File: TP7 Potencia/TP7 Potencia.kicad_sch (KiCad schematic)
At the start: 55 parts, among them J1 Input, Q1 IRF830PBF, Q2 IRF830PBF, Q3 IRF830PBF, Q4 IRF830PBF, Q5 BC337, Q6 BC337, Q7 2N7000, Q8 2N7000, SW1 SW_Push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

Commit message: Agregado footprints
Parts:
- removed U4: CD4049UBEE4, CD4049UBEE4:DIP794W45P254L1969H508Q16, symbol CD4049:CD4049UBEE4
- added U6: CD40106BE, footprints:DIP794W45P254L1969H508Q14, symbol C40106:CD40106BE
- C1, C3, C6, C7: footprint (none) -> Capacitor_THT:CP_Radial_D6.3mm_P2.50mm
- C10, C2, C4, C5: footprint (none) -> Capacitor_THT:C_Disc_D3.0mm_W1.6mm_P2.50mm
- C8, C9: value 100p -> 500p; footprint (none) -> Capacitor_THT:C_Disc_D3.0mm_W1.6mm_P2.50mm
- D10: footprint (none) -> LED_THT:LED_D3.0mm
- D9: footprint (none) -> Diode_THT:D_DO-35_SOD27_P7.62mm_Horizontal
- J1: footprint (none) -> TerminalBlock_MetzConnect:TerminalBlock_MetzConnect_Type011_RT05502HBWC_1x02_P5.00mm_Horizontal
- Q1, Q2, Q3, Q4: footprint TO254P1052X465X1989-3 -> footprints:TO254P1052X465X1989-3
- R1, R10, R11, R12, R13, R14, R15, R16, R2, R3, R4, R5, R6, R9: footprint (none) -> Resistor_THT:R_Axial_DIN0207_L6.3mm_D2.5mm_P10.16mm_Horizontal
- R7, R8: value 5k8 -> 12k; footprint (none) -> Resistor_THT:R_Axial_DIN0207_L6.3mm_D2.5mm_P10.16mm_Horizontal
- RV1, RV2, RV3, RV4: footprint (none) -> Potentiometer_THT:Potentiometer_Bourns_3266Y_Vertical
- SW1: footprint (none) -> Button_Switch_THT:SW_Push_2P1T_Toggle_CK_PVA1xxH1xxxxxxV2
- U1: footprint (none) -> Package_DIP:DIP-16_W7.62mm_Socket_LongPads
- U5: footprint (none) -> Package_DIP:DIP-8_W7.62mm_Socket_LongPads
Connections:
- net 12V: now also U6.14 (VDD)
- net B: now also U6.3 (B)
- net D: now also U6.6 (I=~C), U6.9 (D)
- net E: now also U6.11 (E)
- net GND: now also U6.7 (VSS)
- net PWM: now also U6.1 (A), U6.5 (C)
- net PWM1: now also U6.4 (H=~B)
- net PWM2: now also U6.10 (K=~E)
- net at D8.2 (A), R8.1: now also U6.8 (J=~D)
- net at D7.2 (A), R7.1: now also U6.2 (G=~A)
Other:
- note removed: "AGREGAR FOOTPRINTS Y CHECKEAR BIEN QUE SEAN LOS CORRECTOS"
- moved on the sheet: C10, D10, Q5, Q6, Q7, Q8, R12, R13, R14, R15, R16, SW1

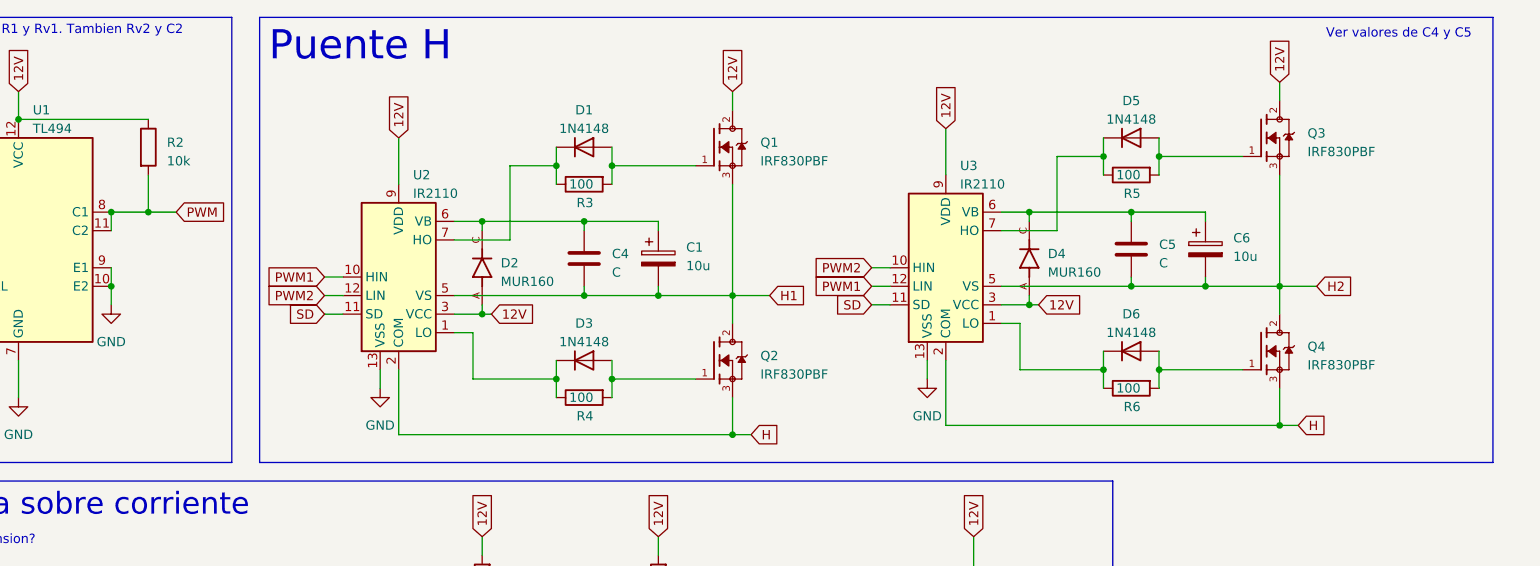
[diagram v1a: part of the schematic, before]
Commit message: Placement de componentes en el PCB
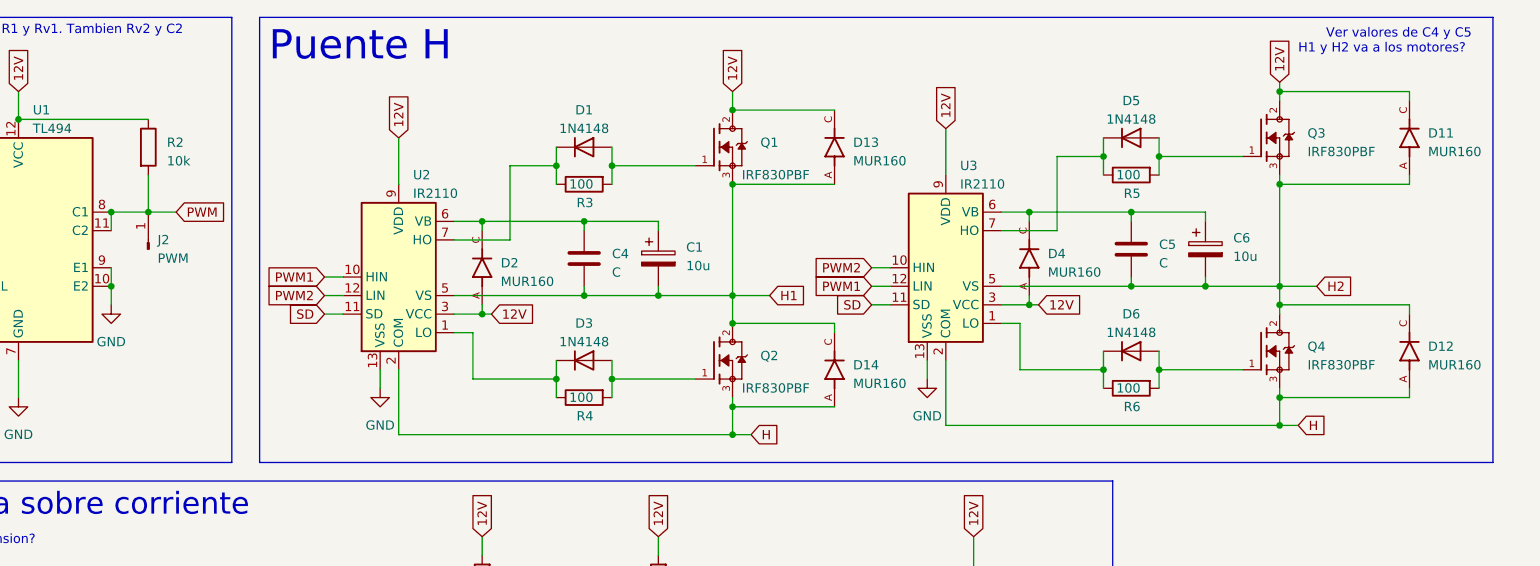
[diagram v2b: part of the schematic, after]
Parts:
- added D11, D12, D13, D14: MUR160, MUR160:DIOAD1300W80L670D310, symbol MUR160:MUR160
- added J2: PWM, Connector_PinSocket_2.54mm:PinSocket_1x01_P2.54mm_Vertical, symbol Connector:Conn_01x01_Pin
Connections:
- net 12V: now also D11.C, D13.C
- net H: now also D12.A, D14.A
- net H1: now also D13.A, D14.C
- net H2: now also D11.A, D12.C
- net PWM: now also J2.1 (Pin_1)
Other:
- note added: "H1 y H2 va a los motores?"

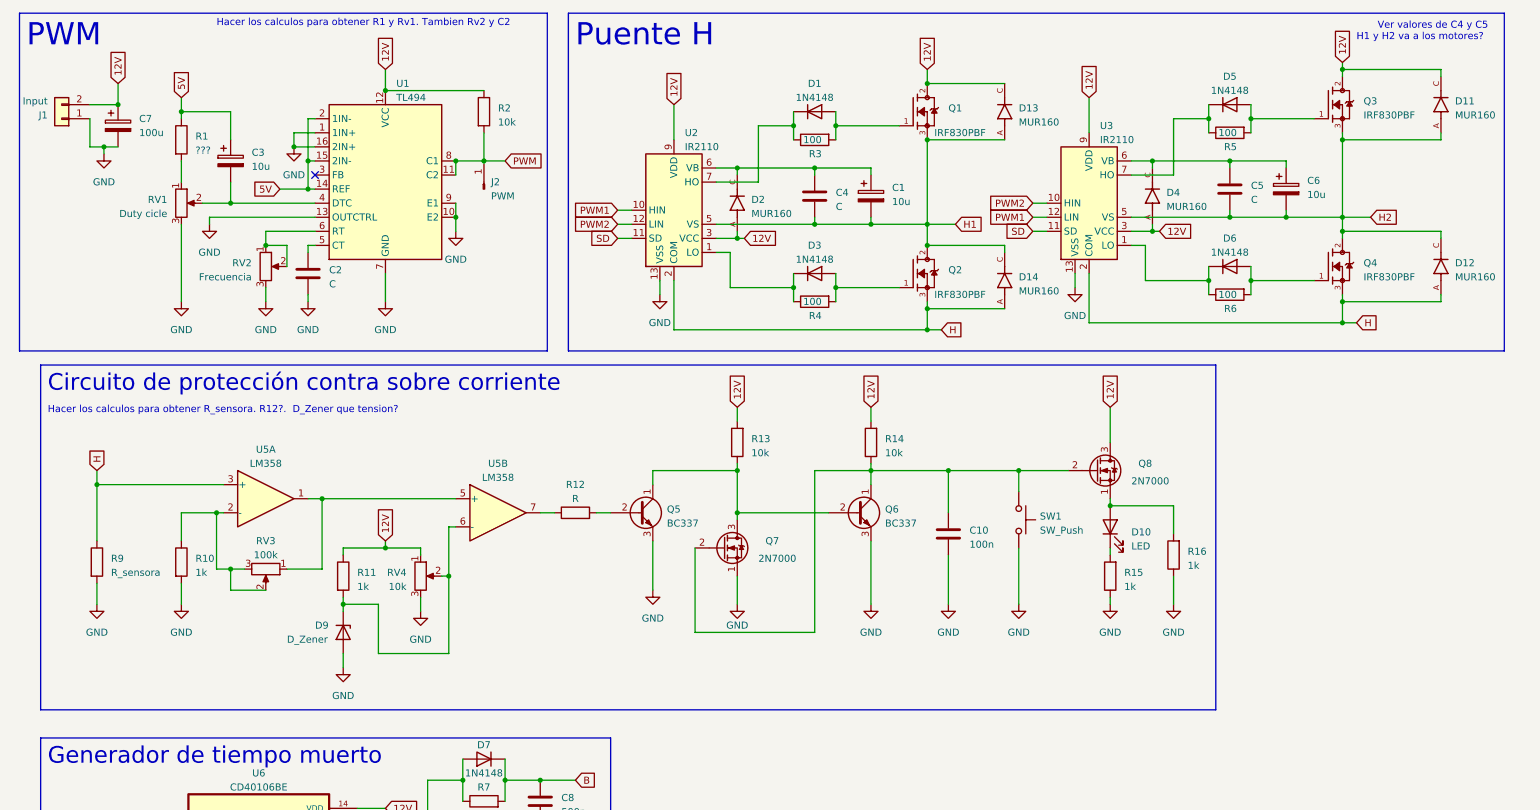
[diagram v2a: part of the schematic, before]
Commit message: Ordenados los componentes por bloques
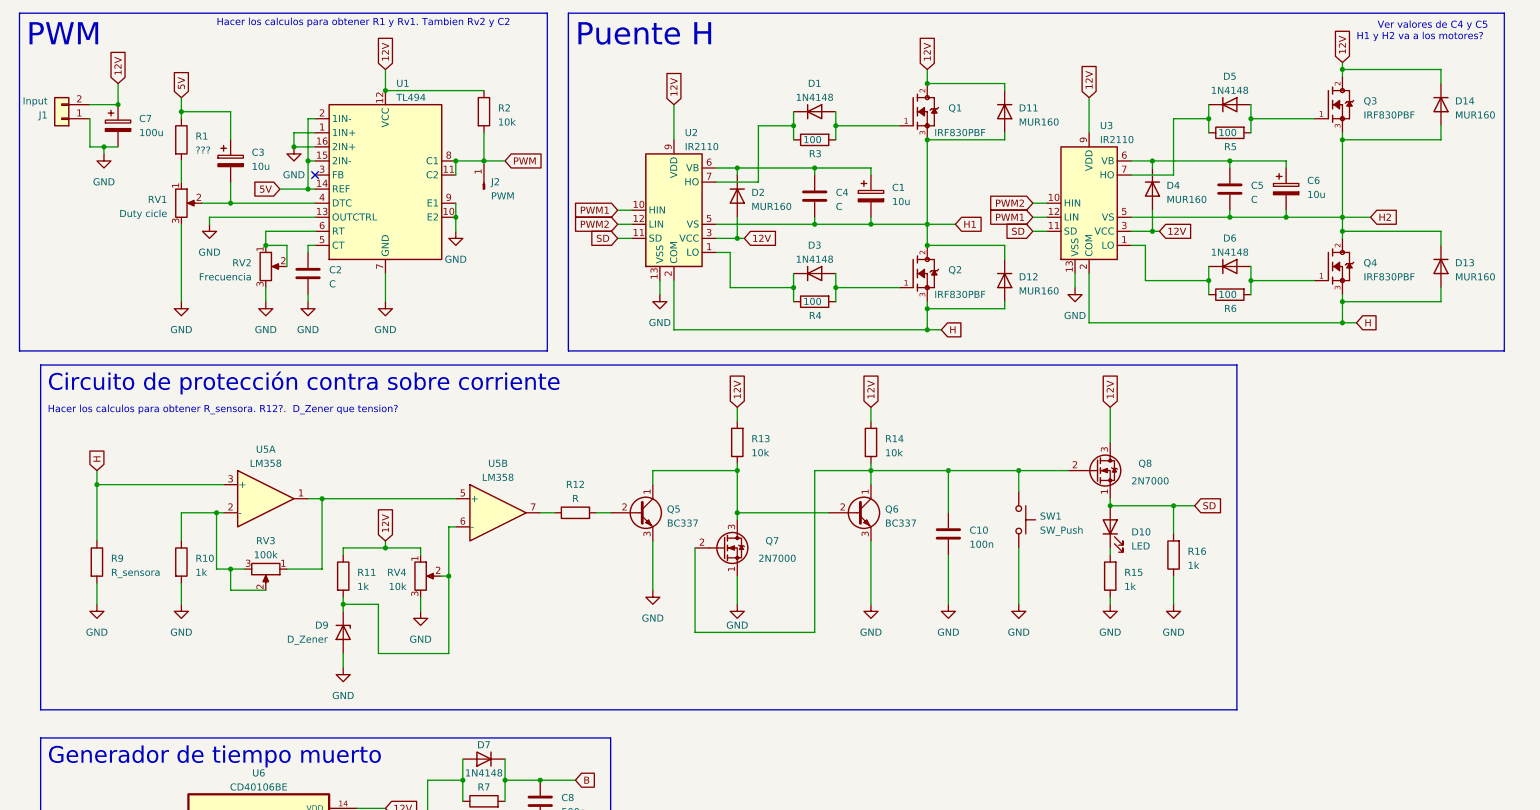
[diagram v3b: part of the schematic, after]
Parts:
- removed D11, D12, D13, D14, D2, D4: MUR160, MUR160:DIOAD1300W80L670D310, symbol MUR160:MUR160
- added D11, D12, D13, D14, D2, D4: MUR160, Diode_THT:D_DO-35_SOD27_P7.62mm_Horizontal, symbol Diode:1N4148
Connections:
- net 12V: now also D11.1 (K), D14.1 (K), D2.2 (A), D4.2 (A)
- net H: now also D12.2 (A), D13.2 (A)
- net H1: now also D11.2 (A), D12.1 (K)
- net H2: now also D13.1 (K), D14.2 (A)
- net SD: now also D10.2 (A), Q8.1 (S), R16.2
- net at C5.1, C6.1, U3.6 (VB): now also D4.1 (K)
- net at C1.1, C4.1, U2.6 (VB): now also D2.1 (K)

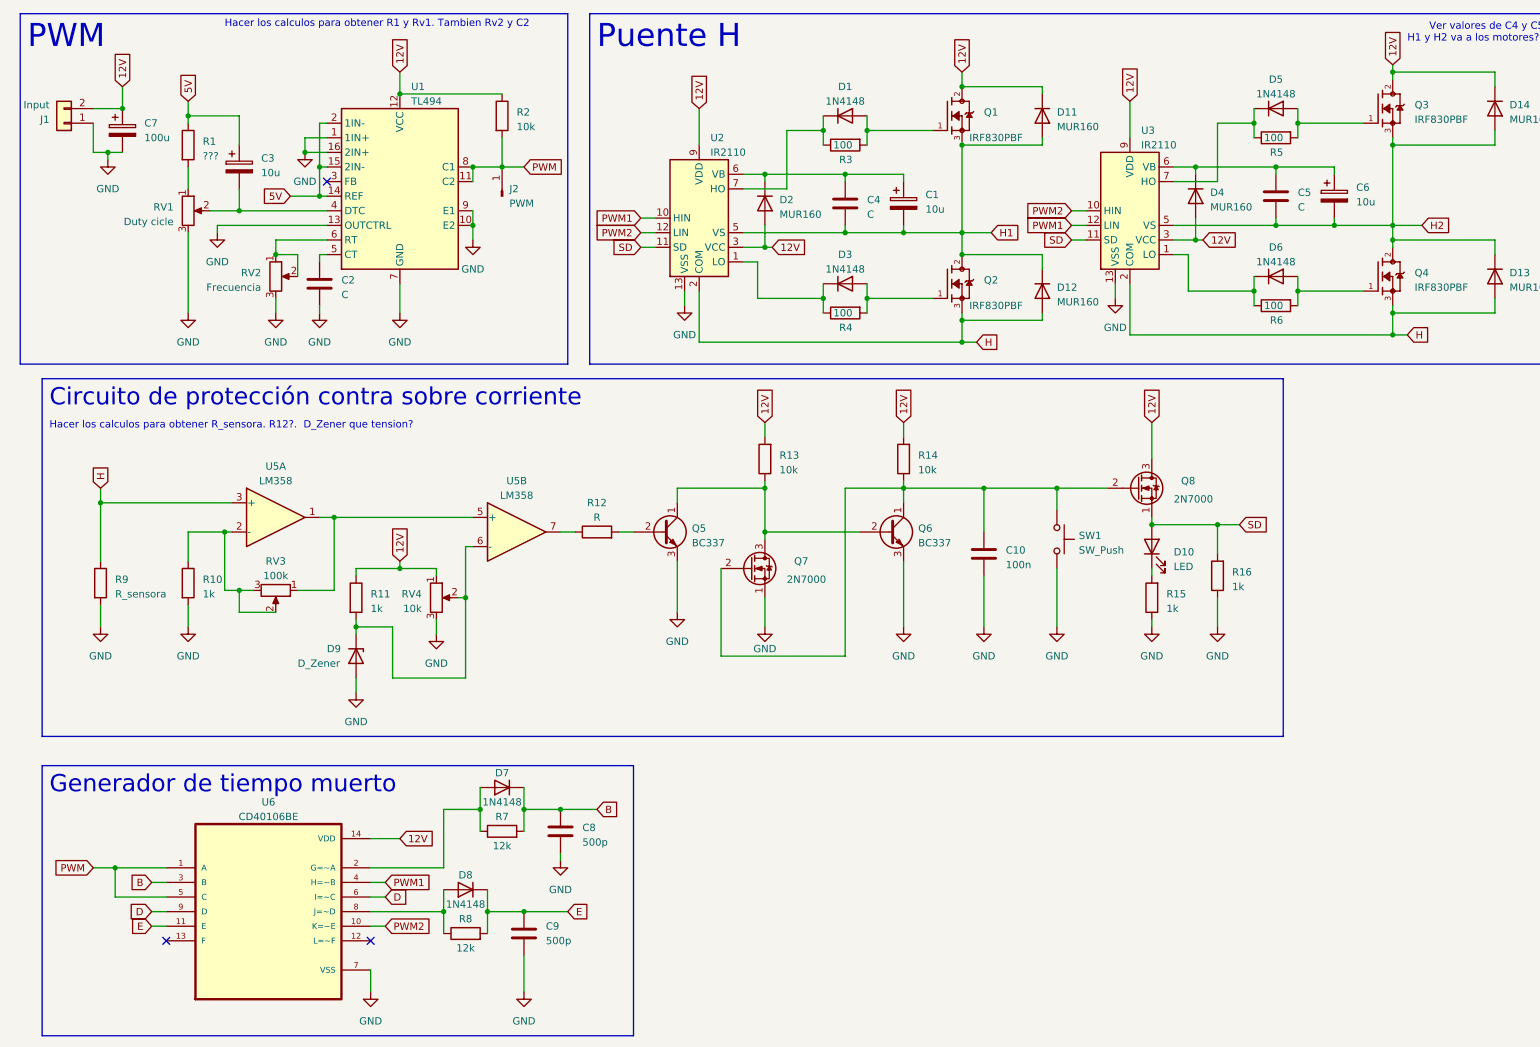
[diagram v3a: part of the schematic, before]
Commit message: continuacion del rooteo y agregado de testpoint y borneras
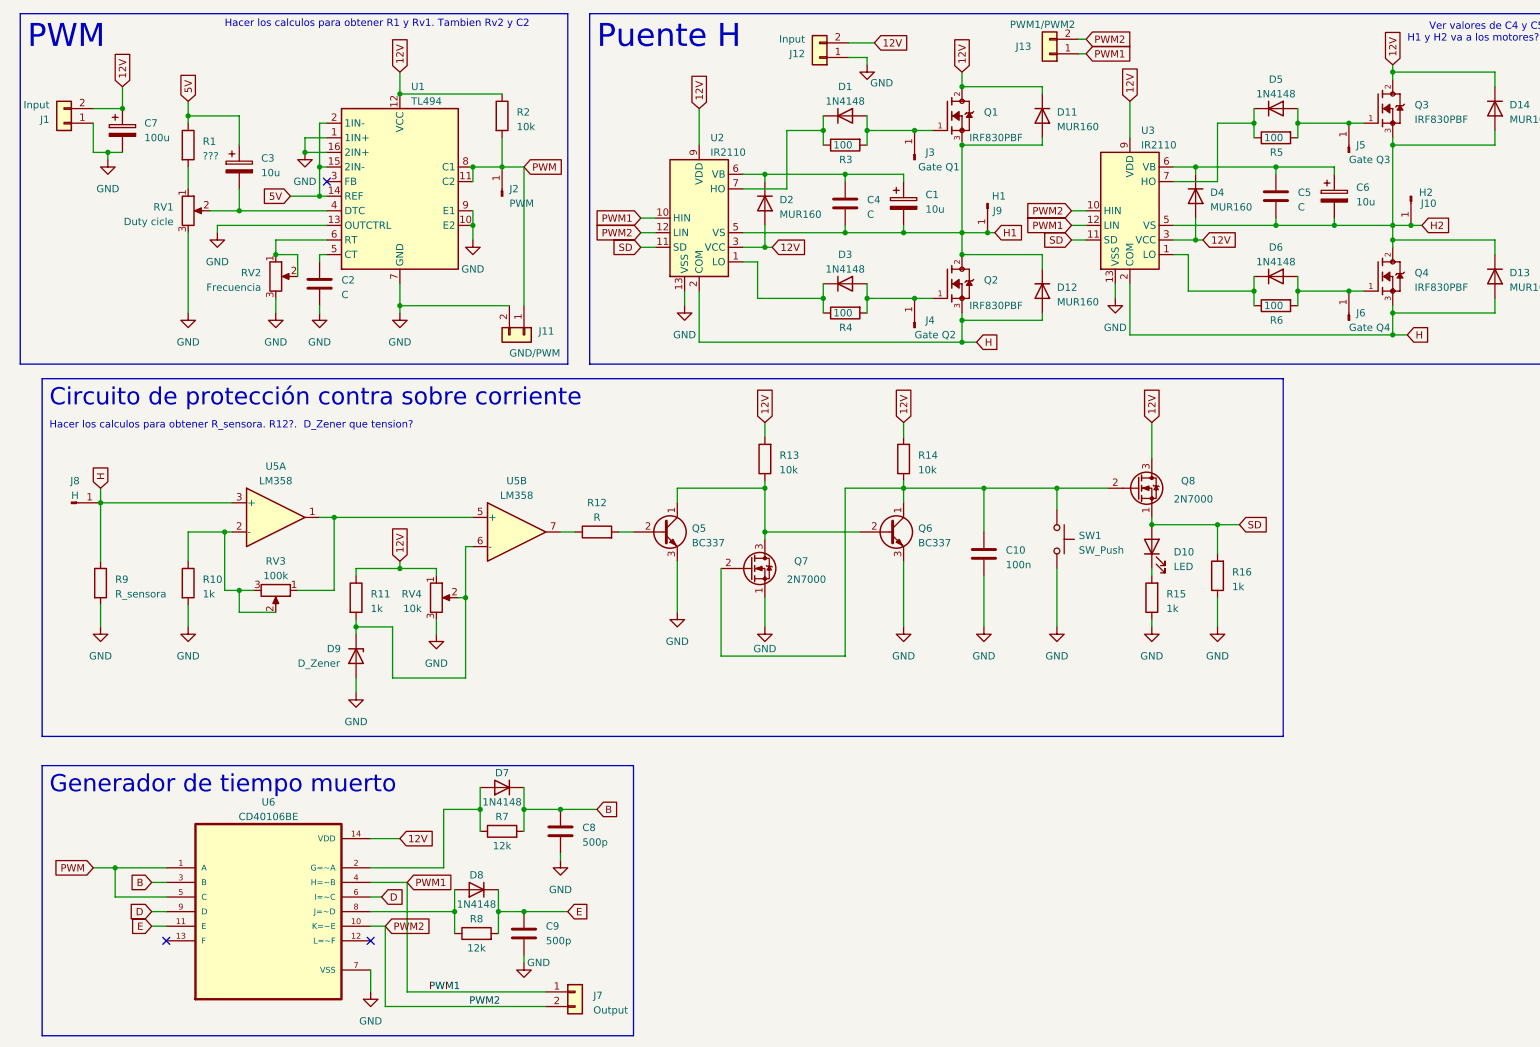
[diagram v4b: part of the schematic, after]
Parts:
- added J10: H2, Connector_PinSocket_2.54mm:PinSocket_1x01_P2.54mm_Vertical, symbol Connector:Conn_01x01_Pin
- added J11: GND/PWM, TerminalBlock_MetzConnect:TerminalBlock_MetzConnect_Type011_RT05502HBWC_1x02_P5.00mm_Horizontal, symbol Connector_Generic:Conn_01x02
- added J12: Input, TerminalBlock_MetzConnect:TerminalBlock_MetzConnect_Type011_RT05502HBWC_1x02_P5.00mm_Horizontal, symbol Connector_Generic:Conn_01x02
- added J13: PWM1/PWM2, TerminalBlock_MetzConnect:TerminalBlock_MetzConnect_Type011_RT05502HBWC_1x02_P5.00mm_Horizontal, symbol Connector_Generic:Conn_01x02
- added J3: Gate Q1, Connector_PinSocket_2.54mm:PinSocket_1x01_P2.54mm_Vertical, symbol Connector:Conn_01x01_Pin
- added J4: Gate Q2, Connector_PinSocket_2.54mm:PinSocket_1x01_P2.54mm_Vertical, symbol Connector:Conn_01x01_Pin
- added J5: Gate Q3, Connector_PinSocket_2.54mm:PinSocket_1x01_P2.54mm_Vertical, symbol Connector:Conn_01x01_Pin
- added J6: Gate Q4, Connector_PinSocket_2.54mm:PinSocket_1x01_P2.54mm_Vertical, symbol Connector:Conn_01x01_Pin
- added J7: Output, TerminalBlock_MetzConnect:TerminalBlock_MetzConnect_Type011_RT05502HBWC_1x02_P5.00mm_Horizontal, symbol Connector_Generic:Conn_01x02
- added J8: H, Connector_PinSocket_2.54mm:PinSocket_1x01_P2.54mm_Vertical, symbol Connector:Conn_01x01_Pin
- added J9: H1, Connector_PinSocket_2.54mm:PinSocket_1x01_P2.54mm_Vertical, symbol Connector:Conn_01x01_Pin
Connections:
- net 12V: now also J12.2 (Pin_2)
- net GND: now also J11.2 (Pin_2), J12.1 (Pin_1)
- net H: now also J8.1 (Pin_1)
- net H1: now also J9.1 (Pin_1)
- net H2: now also J10.1 (Pin_1)
- net PWM: now also J11.1 (Pin_1)
- net PWM1: now also J13.1 (Pin_1), J7.1 (Pin_1)
- net PWM2: now also J13.2 (Pin_2), J7.2 (Pin_2)
- net at D1.2 (A), Q1.1, R3.2: now also J3.1 (Pin_1)
- net at D3.2 (A), Q2.1, R4.2: now also J4.1 (Pin_1)
- net at D5.2 (A), Q3.1, R5.2: now also J5.1 (Pin_1)
- net at D6.2 (A), Q4.1, R6.2: now also J6.1 (Pin_1)
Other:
- moved on the sheet: D8, R8

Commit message: fin del rooteo
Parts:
- RV1: footprint Potentiometer_THT:Potentiometer_Bourns_3266Y_Vertical -> Potentiometer_THT:Potentiometer_Alps_RK163_Single_Horizontal
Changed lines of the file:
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@@
   )
   (text "Hacer los calculos para obtener R1 y Rv1. Tambien Rv2 y C2"
-    (at 49.53 20.32 0)
+    (at 46.99 20.32 0)
     (effects (font (size 1.27 1.27)) (justify left bottom))
   )
@@
       (effects (font (size 1.27 1.27)) (justify right))
     )
-    (property "Footprint" "Potentiometer_THT:Potentiometer_Bourns_3266Y_Vertical" (at 43.18 52.07 0)
-      (effects (font (size 1.27 1.27)) hide)
-    )
+    (property "Footprint" "Potentiometer_THT:Potentiometer_Alps_RK163_Single_Horizontal" (at 43.18 52.07 0)
+      (effects (font (size 1.27 1.27)) hide)
+    )
